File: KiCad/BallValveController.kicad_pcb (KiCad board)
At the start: 2 copper layers, 55.6 x 43.2 mm, 61 parts, among them J1 Screw_Terminal_01x03, J2 Screw_Terminal_01x04, J3 Screw_Terminal_01x04, J4 Screw_Terminal_01x04, J5 Conn_01x01_Male, J6 Screw_Terminal_01x04, J7 Screw_Terminal_01x02, K1 G5V-2, Q1 Q_PMOS_GDS, Q2 2N2222A, U1 MT2499A, U2 L7805, U3 XIAO-ESP32-C6

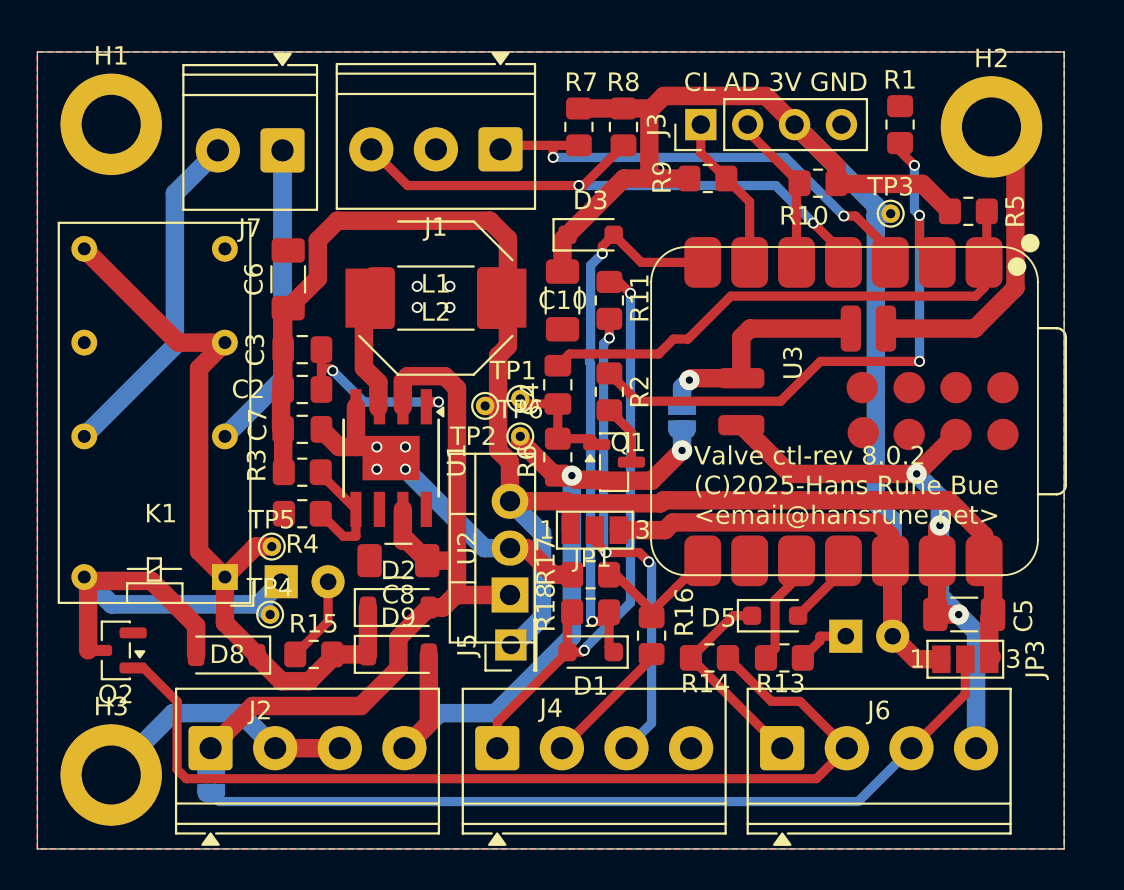
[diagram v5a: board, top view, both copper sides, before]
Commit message: Fixed MT2499A layout
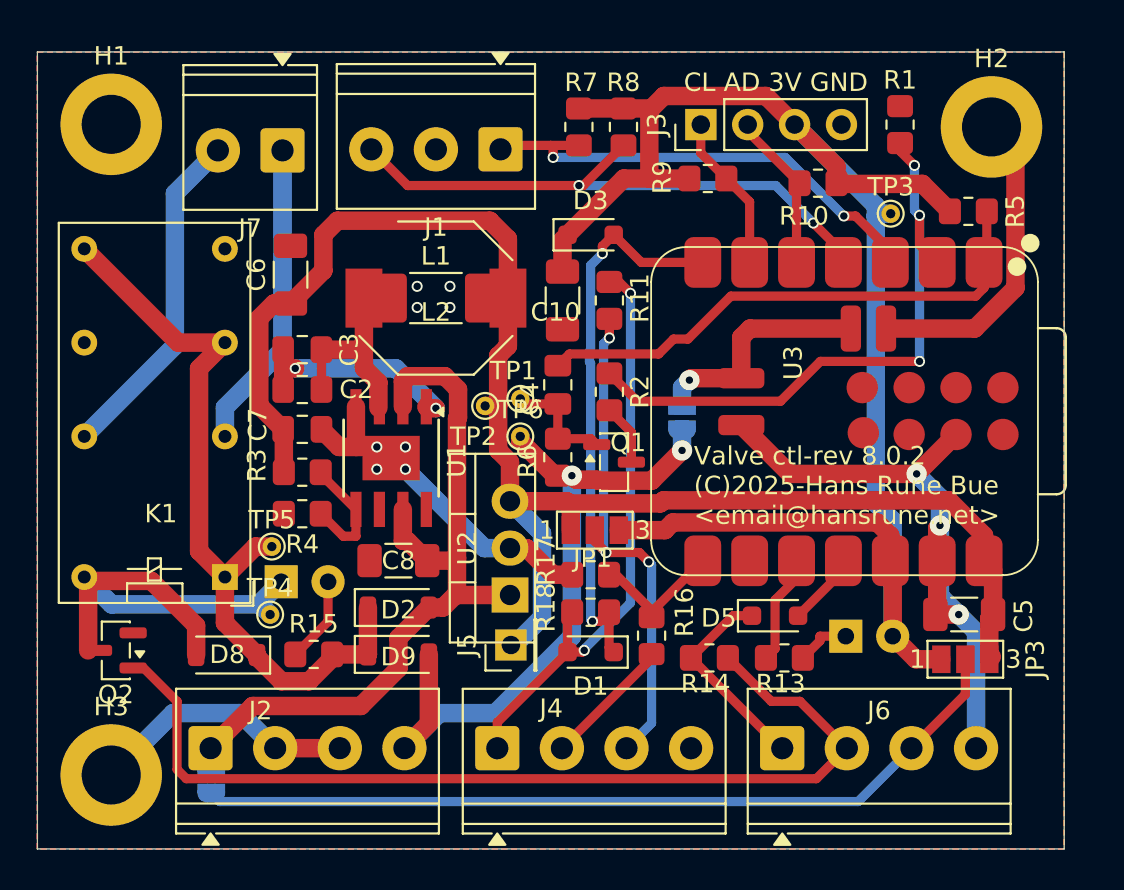
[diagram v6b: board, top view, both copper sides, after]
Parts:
- L1: value L -> 10uH; footprint Inductor_SMD:L_2512_6332Metric_Pad1.52x3.35mm_HandSolder -> Inductor_SMD:L_2010_5025Metric_Pad1.52x2.65mm_HandSolder
- L2: value L -> 22uH
- R3: value 88k7 -> 68k
- R4: value 20k -> 15k
- moved C6 0.28 mm to (149.6, 93.2)
- turned C2 to 0 degrees
- turned C3 to 0 degrees
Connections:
- C2 pad 2: +5V -> /IND1
- C3 pad 2: +5V -> /IND1
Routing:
- net /IND1: track 7.82 -> 12.3 mm
- net Net-(U1-BS): track 10.0 -> 11.9 mm
- net +5V: track 85.5 -> 87.0 mm

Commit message: DRC with TPC561201/08
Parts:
- removed C3: 22nF, Capacitor_SMD:C_0805_2012Metric_Pad1.18x1.45mm_HandSolder
- removed U1: MT2499A, Package_SO:TI_SO-PowerPAD-8
- added U4: TPS561201 or 08, Package_TO_SOT_SMD:SOT-23-6, F.Cu at (151.9, 105.4)
- L1: value 10uH -> 4.7uH
- L2: value 22uH -> 10uH
- R4: value 15k -> 12k
- moved TP5 21.4 mm to (138.3, 89.2)
- moved C6 11.1 mm to (160.5, 95.2), turned to 0 degrees
- moved C7 10.9 mm to (160.4, 97.7)
- moved L1 6.28 mm to (152.7, 98.6)
- moved L2 6.28 mm to (152.7, 98.6)
- moved C2 5.79 mm to (148.7, 105.0), turned to 90 degrees
- moved R3 5.73 mm to (156.0, 104.3), turned to 180 degrees
- moved R4 5.72 mm to (156.0, 106.4), turned to 0 degrees
- moved TP2 1.31 mm to (159.5, 101.5)
- turned C8 to 0 degrees
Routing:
- net +5V: track 87.0 -> 61.7 mm
- net GND: track 90.2 -> 112.8 mm, vias 11 -> 7
- net /IND1: track 12.3 -> 22.1 mm, vias 0 -> 4
- net /PwrIn: track 41.7 -> 33.4 mm, vias 0 -> 2
- net Net-(U4-VBST): track 11.9 -> 7.08 mm
- net Net-(U4-VFB): track 6.67 -> 4.11 mm
- net +VSW: track 41.7 -> 40.6 mm
- net /ILow: track 51.9 -> 52.6 mm
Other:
- board text added: "Valve ctl-rev 8.1.0 (C)2025-Hans Rune Bue <email@hansrune.net>"

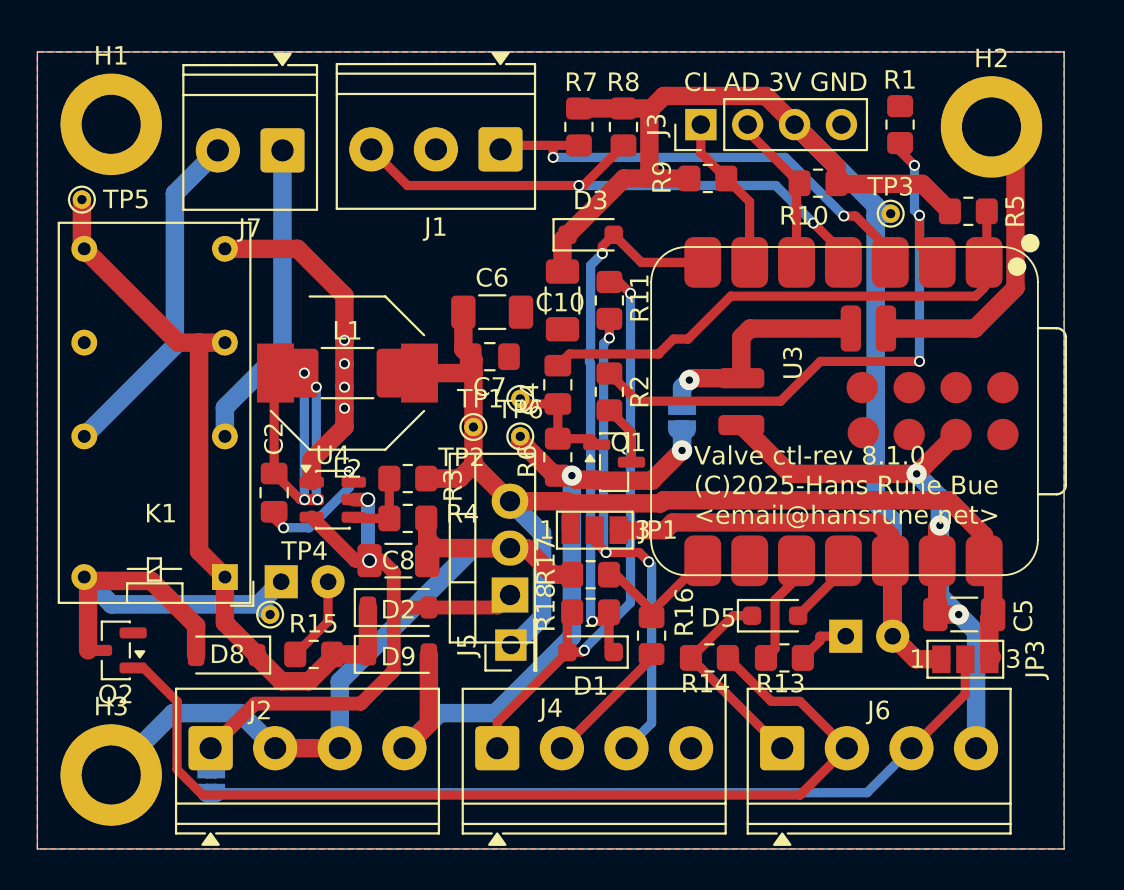
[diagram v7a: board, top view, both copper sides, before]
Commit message: Added EN resistor for buck converter
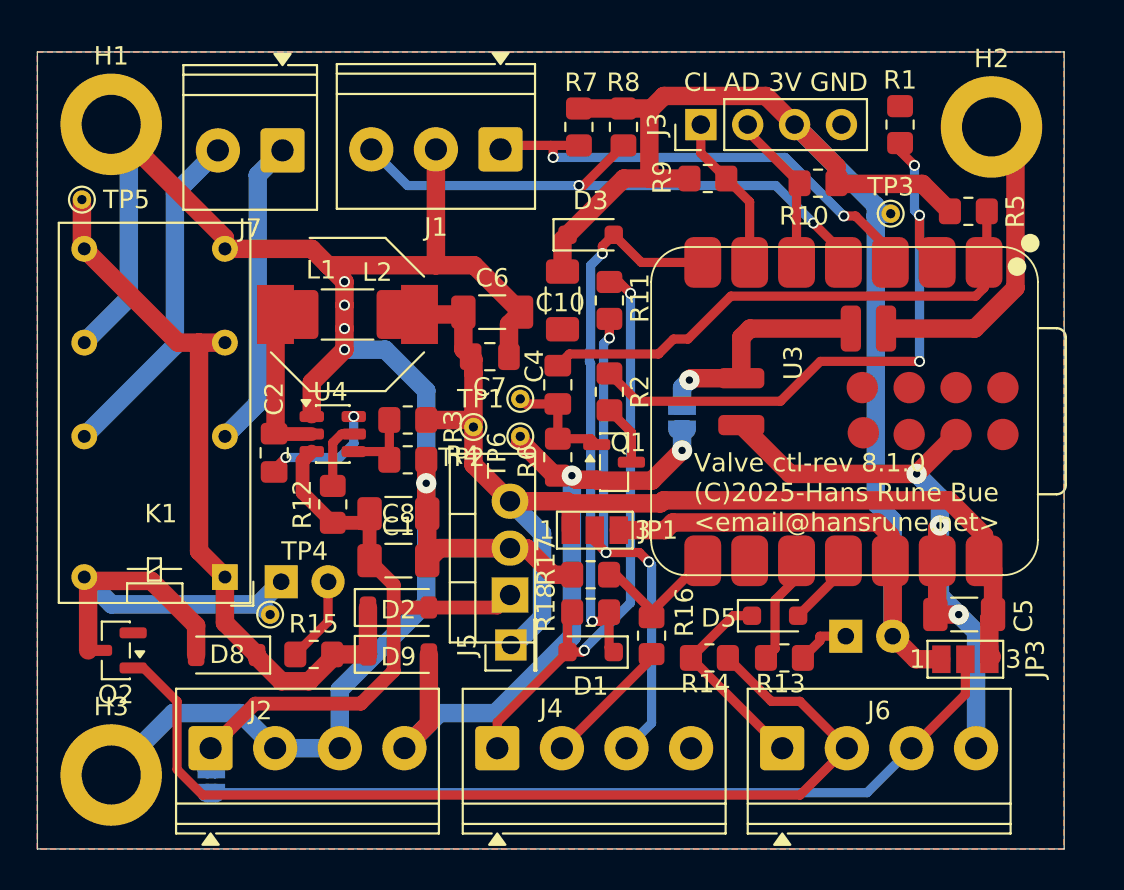
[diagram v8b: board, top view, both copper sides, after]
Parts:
- added C1: 22uF, Capacitor_SMD:C_1206_3216Metric_Pad1.33x1.80mm_HandSolder, F.Cu at (155.4, 108.7)
- added R12: 10k, Resistor_SMD:R_0805_2012Metric_Pad1.20x1.40mm_HandSolder, F.Cu at (151.9, 105.7)
- U4: value TPS561201 or 08 -> TPS561201/08 or TPS563200
- moved U4 3.56 mm to (151.9, 101.9)
- moved L1 3.18 mm to (152.7, 95.4)
- moved L2 3.18 mm to (152.7, 95.4)
- moved R3 3.17 mm to (156.0, 101.1)
- moved R4 3.17 mm to (156.0, 103.3)
- moved C8 2.54 mm to (155.4, 106.2)
- moved C2 2.16 mm to (148.7, 102.9)
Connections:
- U4 pad 5: /PwrIn -> Net-(U4-EN)
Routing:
- net GND: track 112.8 -> 171.3 mm, vias 7 -> 8
- net /IND1: track 22.1 -> 8.68 mm, vias 4 -> 0
- net Net-(U4-EN): track 0.00 -> 3.67 mm
- net /PwrIn: track 33.4 -> 34.2 mm, vias 2 -> 0
- net +5V: track 61.7 -> 60.9 mm
- net Net-(U4-VBST): track 7.08 -> 6.51 mm
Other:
- board text removed: "Valve ctl-rev 8.0.2 (C)2025-Hans Rune Bue <email@hansrune.net>"
